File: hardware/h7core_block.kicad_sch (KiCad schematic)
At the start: 74 parts, among them J1 USB-C, J3 TC2030-NL SWD, U1 STM32H743VIT6, U3 AP63203WU-7, U4 TLV75533PDBVR, U6 PCM5102APWR, U8 PCM1808PWR, Y1 25MHz 12pF

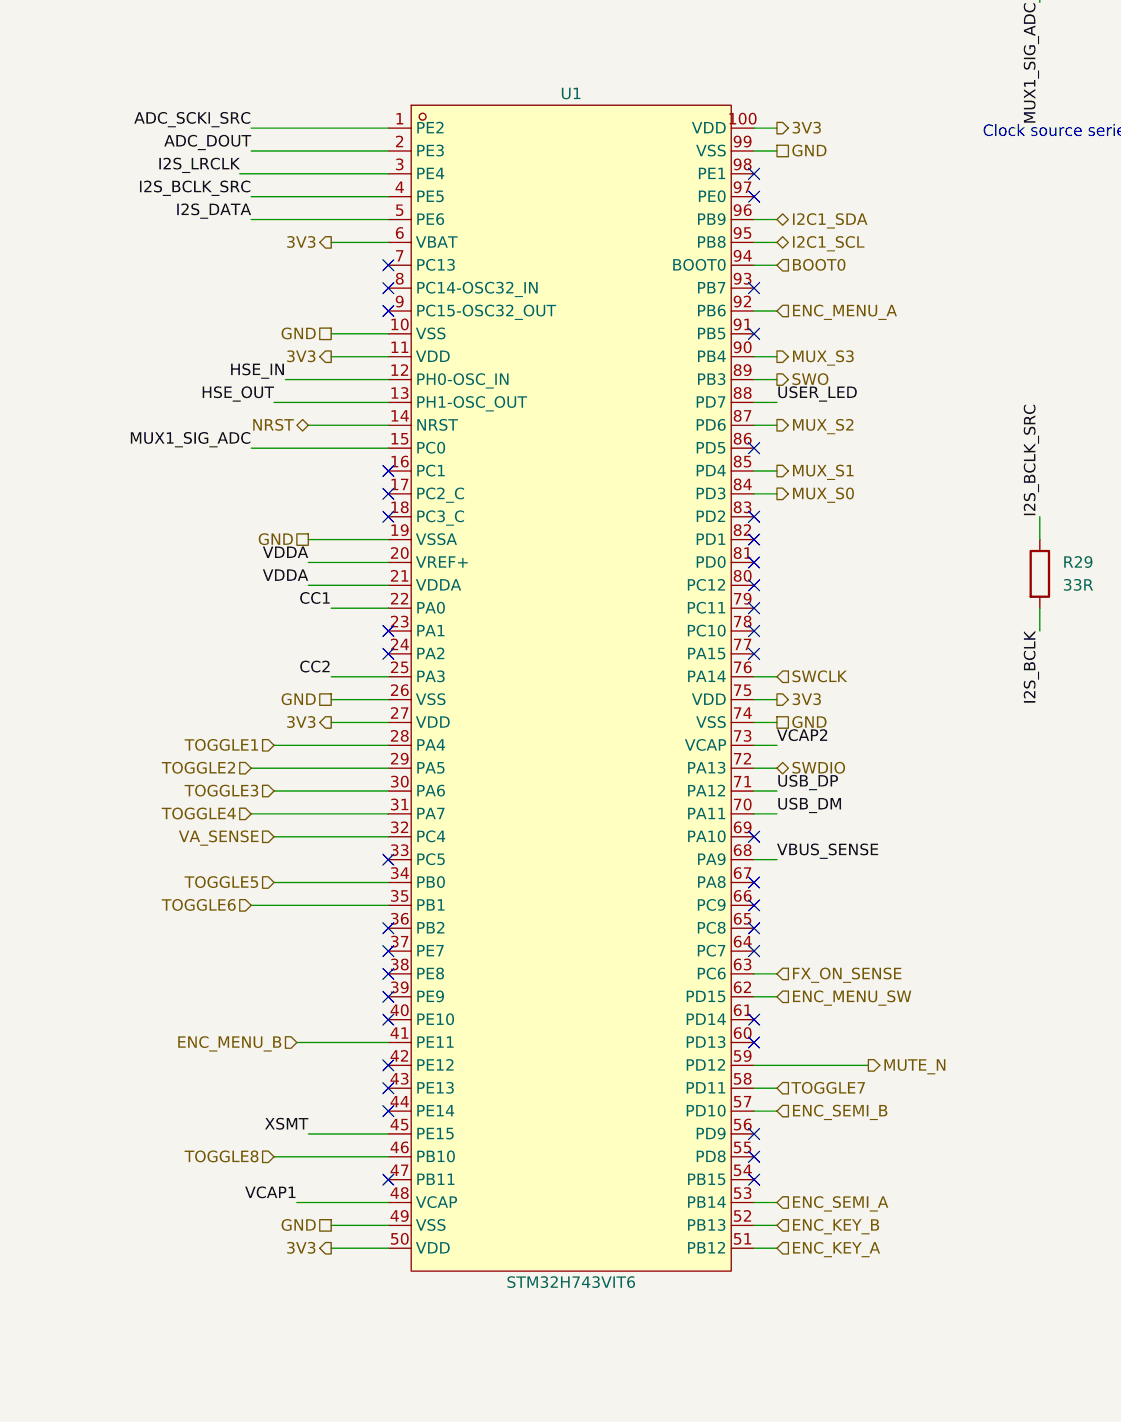
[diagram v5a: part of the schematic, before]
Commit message: feat(hardware): reassign MCU pins to the edge facing each destination
The old map left 14 of 35 local nets on the U1 edge facing away from
their parts. Each movable net now leaves the facing edge in fan-out
order, I2C moves to I2C2 on the OLED corner, CC1/CC2 come off the MCU
(USB is data only) and MUTE_N avoids the JTAG pull-up pins. The
VA_SENSE divider moves beside U106's 5VA pin with its cap at the MCU.
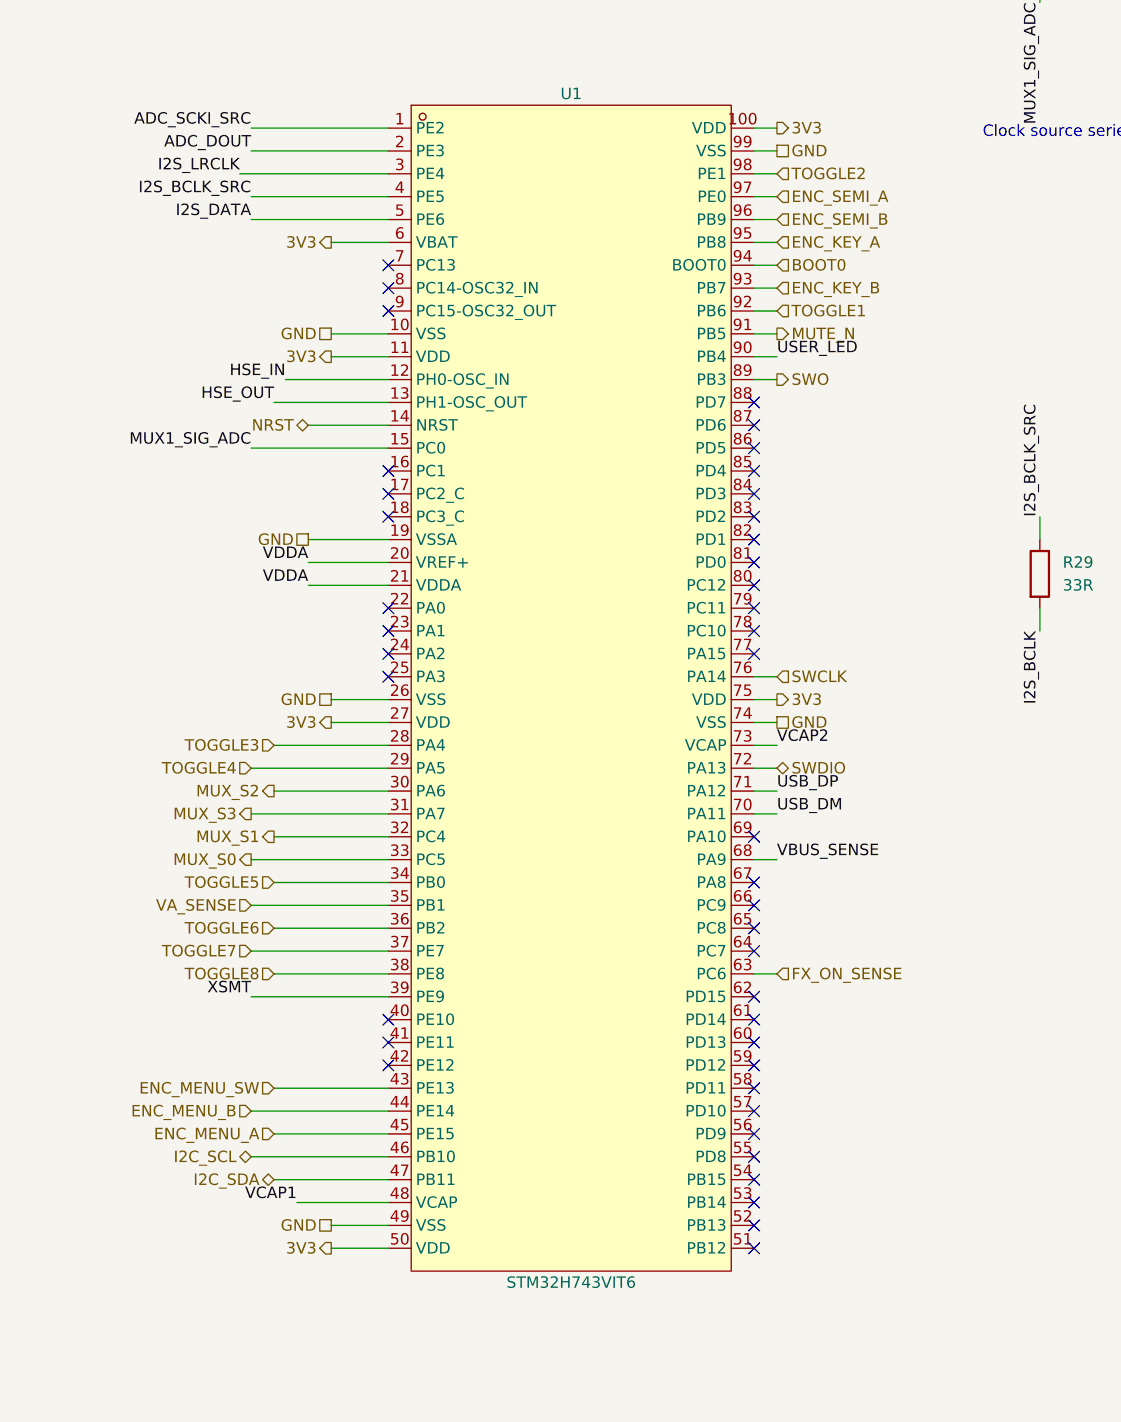
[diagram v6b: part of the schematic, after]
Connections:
- net I2C1_SCL is gone; now on net ENC_KEY_A: U1.95 (PB8)
- net I2C1_SDA is gone; now on net ENC_SEMI_B: U1.96 (PB9)
- net CC1: no longer U1.22 (PA0)
- net CC2: no longer U1.25 (PA3)
- net ENC_KEY_A: no longer U1.51 (PB12)
- net ENC_KEY_B: now also U1.93 (PB7); no longer U1.52 (PB13)
- net ENC_MENU_A: now also U1.45 (PE15); no longer U1.92 (PB6)
- net ENC_MENU_B: now also U1.44 (PE14); no longer U1.41 (PE11)
- net ENC_MENU_SW: now also U1.43 (PE13); no longer U1.62 (PD15)
- net ENC_SEMI_A: now also U1.97 (PE0); no longer U1.53 (PB14)
- net ENC_SEMI_B: no longer U1.57 (PD10)
- net MUTE_N: now also U1.91 (PB5); no longer U1.59 (PD12)
- net MUX_S0: now also U1.33 (PC5); no longer U1.84 (PD3)
- net MUX_S1: now also U1.32 (PC4); no longer U1.85 (PD4)
- net MUX_S2: now also U1.30 (PA6); no longer U1.87 (PD6)
- net MUX_S3: now also U1.31 (PA7); no longer U1.90 (PB4)
- net TOGGLE1: now also U1.92 (PB6); no longer U1.28 (PA4)
- net TOGGLE2: now also U1.98 (PE1); no longer U1.29 (PA5)
- net TOGGLE3: now also U1.28 (PA4); no longer U1.30 (PA6)
- net TOGGLE4: now also U1.29 (PA5); no longer U1.31 (PA7)
- net TOGGLE6: now also U1.36 (PB2); no longer U1.35 (PB1)
- net TOGGLE7: now also U1.37 (PE7); no longer U1.58 (PD11)
- net TOGGLE8: now also U1.38 (PE8); no longer U1.46 (PB10)
- net USER_LED: now also U1.90 (PB4); no longer U1.88 (PD7)
- net VA_SENSE: now also U1.35 (PB1); no longer U1.32 (PC4)
- net XSMT: now also U1.39 (PE9); no longer U1.45 (PE15)
- net I2C_SDA: now reaches U1.47 (PB11)
- new net I2C_SCL: U1.46 (PB10)
- no-connect marks 44 -> 46

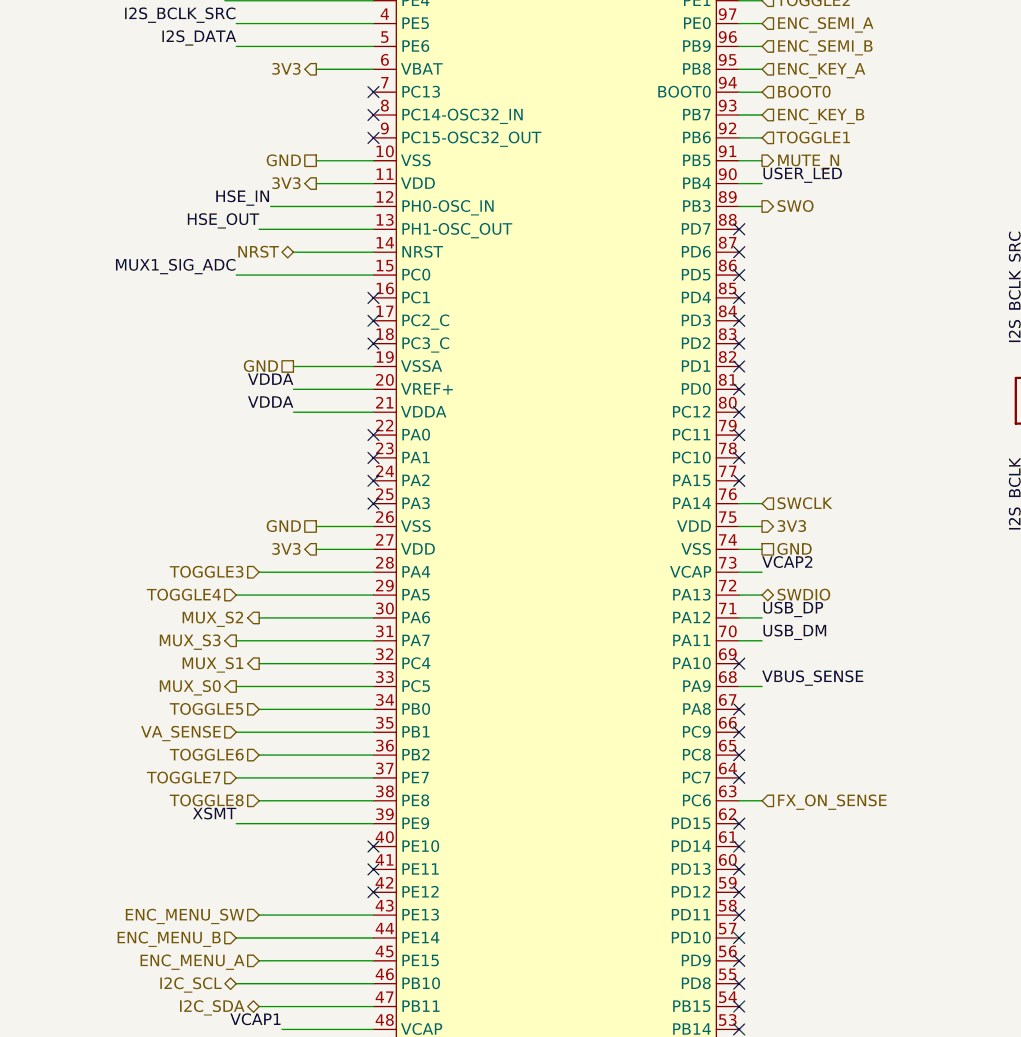
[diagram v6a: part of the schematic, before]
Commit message: feat(layout): clear the U1 west fan-out, divider north of U106
R151/R152/C130 move north of U106, away from the OLED. Each part now
shows one designator. USER_LED moves to PE11 with R3/D1 east of U1, R2
sits at SWBOOT1, R150/R153 swap so MUTE_N enters from below, and C12
turns so the I2C and MENU lines leave the east edge straight.
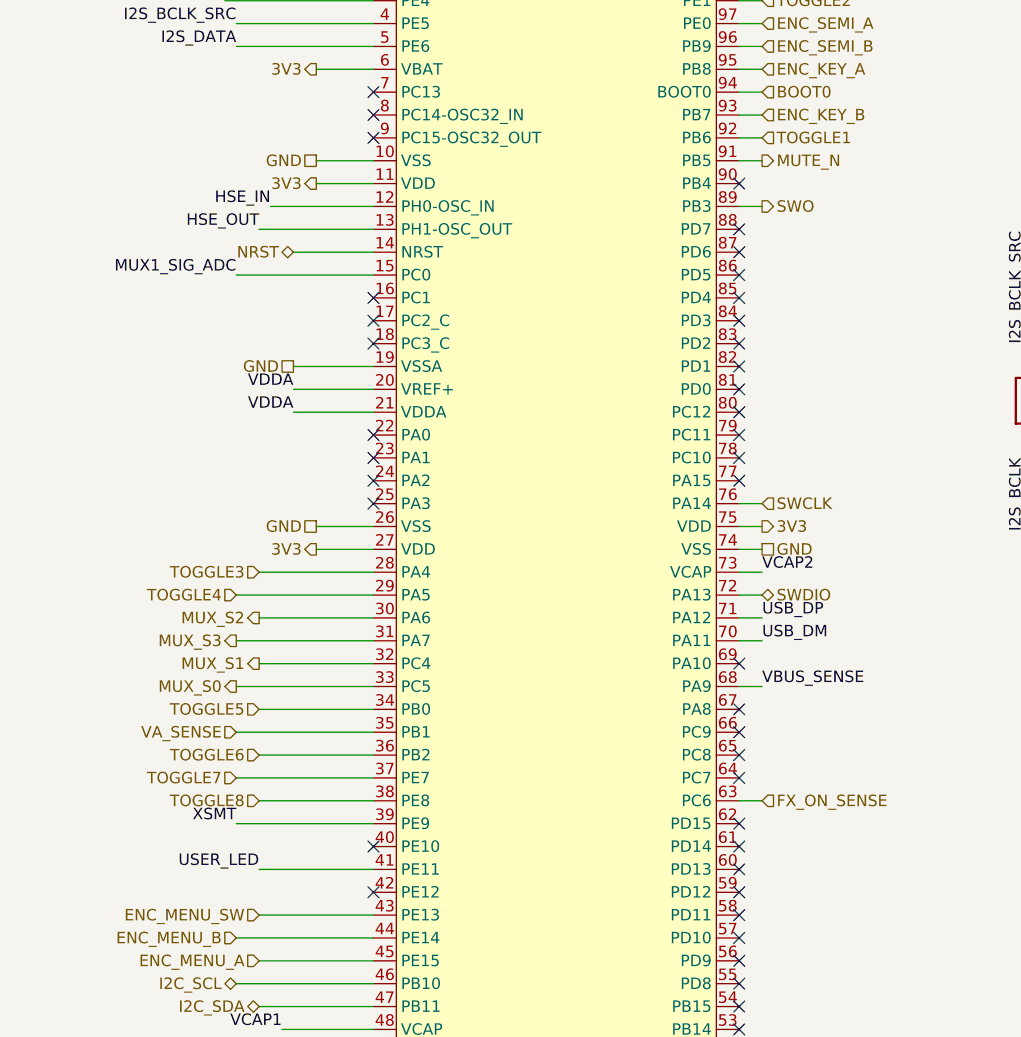
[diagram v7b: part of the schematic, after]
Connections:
- net USER_LED: now also U1.41 (PE11); no longer U1.90 (PB4)
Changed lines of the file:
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@@
 		(at 54.61 176.53)
 	)
-	(no_connect
-		(at 54.61 179.07)
+	(wire
+		(pts
+			(xy 54.61 179.07) (xy 41.91 179.07)
+		)
+		(stroke
+			(width 0)
+			(type default)
+		)
+	)
+	(label "USER_LED"
+		(at 41.91 179.07 180)
+		(fields_autoplaced yes)
+		(effects
+			(font
+				(size 1.27 1.27)
+			)
+			(justify right bottom)
+		)
 	)
 	(no_connect
@@
 		)
 	)
-	(wire
-		(pts
-			(xy 95.25 102.87) (xy 97.79 102.87)
-		)
-		(stroke
-			(width 0)
-			(type default)
-		)
-	)
-	(label "USER_LED"
-		(at 97.79 102.87 0)
-		(fields_autoplaced yes)
-		(effects
-			(font
-				(size 1.27 1.27)
-			)
-			(justify left bottom)
-		)
-	)
-	(wire
+	(no_connect
+		(at 95.25 102.87)
+	)
+	(wire

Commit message: feat(sch): 3V3 decoupler cleanup (C1/C5/C31/C59 deleted, C57/C61 100n, Cx DVDD)
Owner-approved plan layout/3v3_decoupler_plan.md: one 100 nF per VDD pin at pins 50/75, C31/C59 dropped as redundant bulk, new C165 100 nF on PCM5102A DVDD (pin 20).
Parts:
- removed C1, C31, C5: 100nF, Capacitor_SMD:C_0603_1608Metric, symbol Device:C
- removed C59: 10nF, Capacitor_SMD:C_0402_1005Metric, symbol Device:C
- added C165: 100nF, Capacitor_SMD:C_0402_1005Metric, symbol Device:C
- C57, C61: value 10nF -> 100nF; LCSC C15195 -> C1525
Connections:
- net 3V3: now also C165.1
- net GND: now also C165.2
